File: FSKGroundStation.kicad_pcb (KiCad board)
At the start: 4 copper layers, 100 x 82 mm, 206 parts, among them J1 FTSH-105-01-L-DV-K, J10 CX90B1-24P, J11 HTSW-102-07-G-S, J22 BWSMA-KWE-Z001, J23 SJ-3524-SMT, J24 HTSW-103-07-G-S, J25 PJ-063BH, J3 CX90B1-24P, J4 BWSMA-KWE-Z001, J5 BWSMA-KWE-Z001, J9 HTSW-102-07-G-S, Q1 BSS138, Q2 BSS138, U1 TPSM861253RDXR, U10 74LVC1GU04DRL, U2 CC1312R1F3RGZR, U3 CY7C65215-32LTXI, U4 CC1125RHBR, U5 GRF5604, U6 SKYA21003, U7 GRF5604, U8 TPD4E004DRYR, U9 SKYA21003, Y1 OW7EL89CENUYO3YLC-40M, Y2 OW7EL89CANUXK7YLC-48M

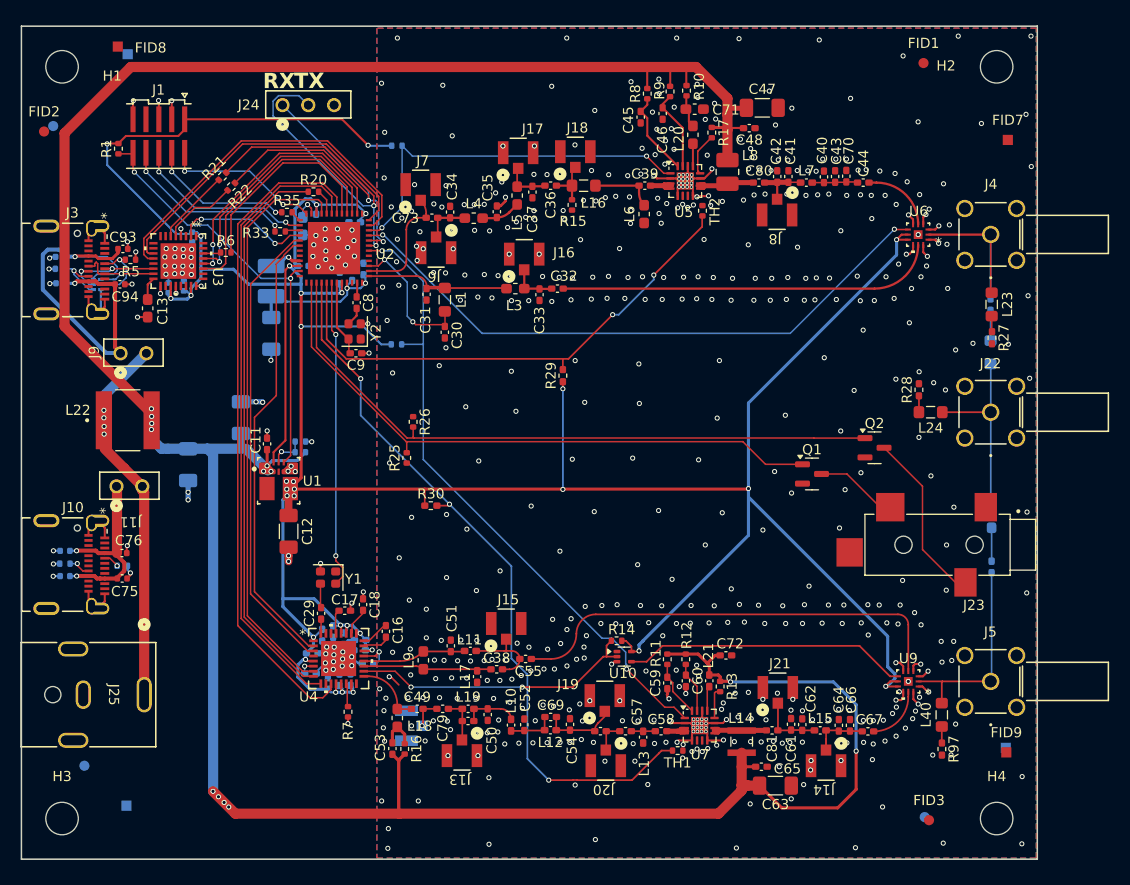
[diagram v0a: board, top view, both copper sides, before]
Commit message: Increase the board width to 82.5mm
To be sure it will work in the chassis.

Signed-off-by: Corey Minyard <corey@minyard.net>
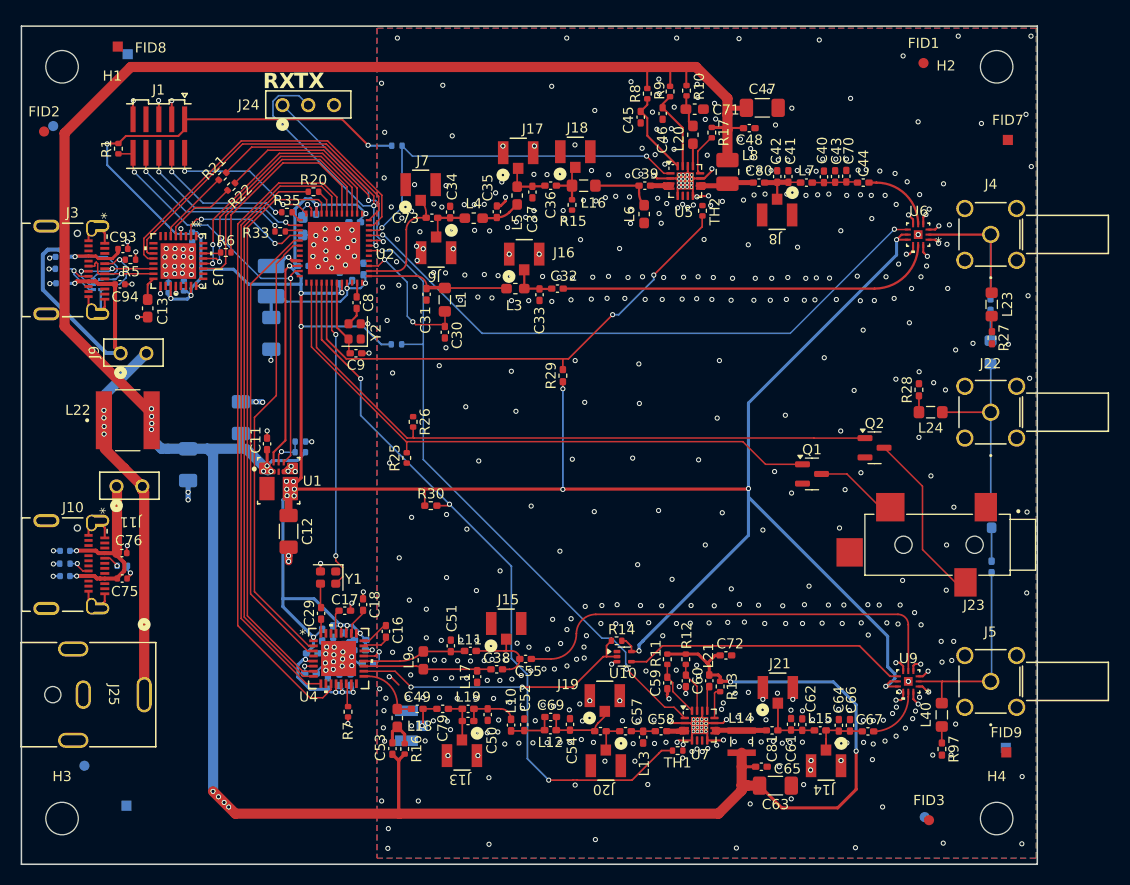
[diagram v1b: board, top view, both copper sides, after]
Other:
- board size 100 x 82 mm -> 100 x 82.5 mm
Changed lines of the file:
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@@
 	)
 	(gr_line
-		(start 170 140)
+		(start 170 140.5)
 		(end 170 58)
 		(stroke
 			(width 0.15)
-			(type default)
+			(type solid)
 		)
 		(locked yes)
@@
 	(gr_line
 		(start 70 58)
-		(end 70 140)
+		(end 70 140.5)
 		(stroke
 			(width 0.15)
-			(type default)
+			(type solid)
 		)
 		(locked yes)
@@
 	)
 	(gr_line
-		(start 70 140)
-		(end 170 140)
+		(start 70 140.5)
+		(end 170 140.5)
 		(stroke
 			(width 0.15)

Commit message: Increase the board width to 83mm
The slot it's supposed to go into is 84mm wide, it appears 82mm in the
middle.  83mm should be good.

According to a post on Amazon, the length is 103mm total with the inside
dimension 100mm.

Signed-off-by: Corey Minyard <corey@minyard.net>
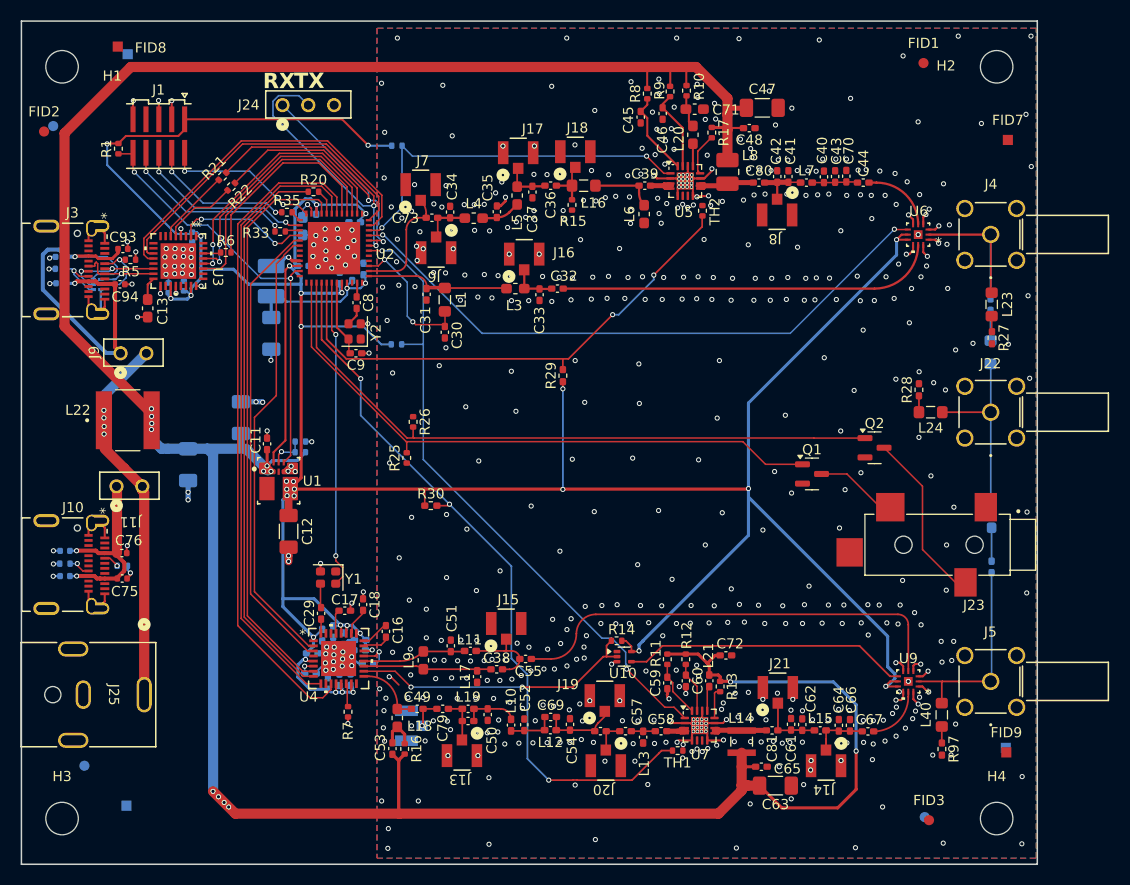
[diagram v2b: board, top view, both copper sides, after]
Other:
- board size 100 x 82.5 mm -> 100 x 83 mm
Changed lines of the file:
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@@
 	(gr_line
 		(start 170 140.5)
-		(end 170 58)
+		(end 170 57.5)
 		(stroke
 			(width 0.15)
@@
 	)
 	(gr_line
-		(start 70 58)
+		(start 70 57.5)
 		(end 70 140.5)
 		(stroke
@@
 	)
 	(gr_line
-		(start 170 58)
-		(end 70 58)
+		(start 170 57.5)
+		(end 70 57.5)
 		(stroke
 			(width 0.15)
-			(type default)
+			(type solid)
 		)
 		(locked yes)

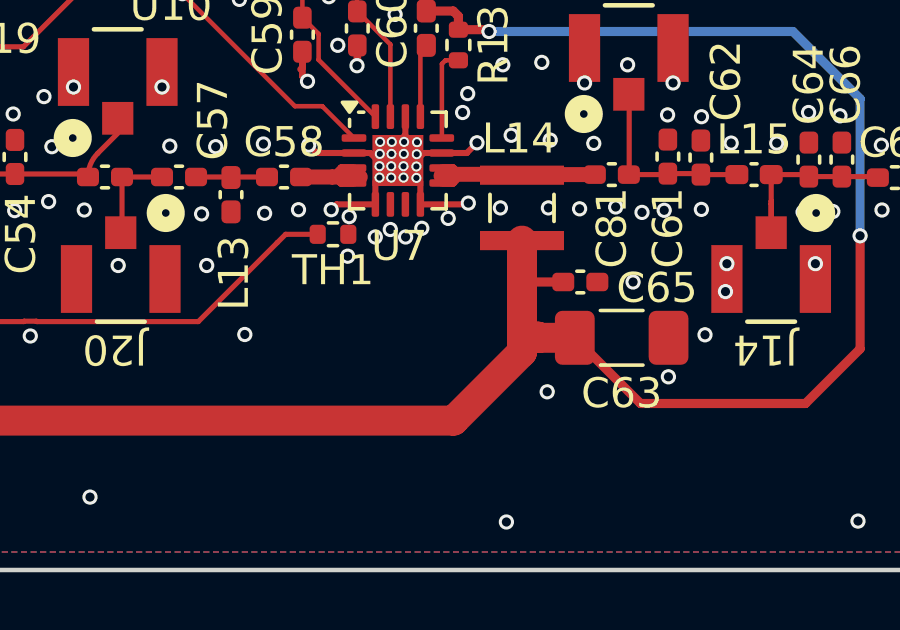
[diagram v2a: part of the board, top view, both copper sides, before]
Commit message: Add some more notes on heat sink options
Signed-off-by: Corey Minyard <corey@minyard.net>
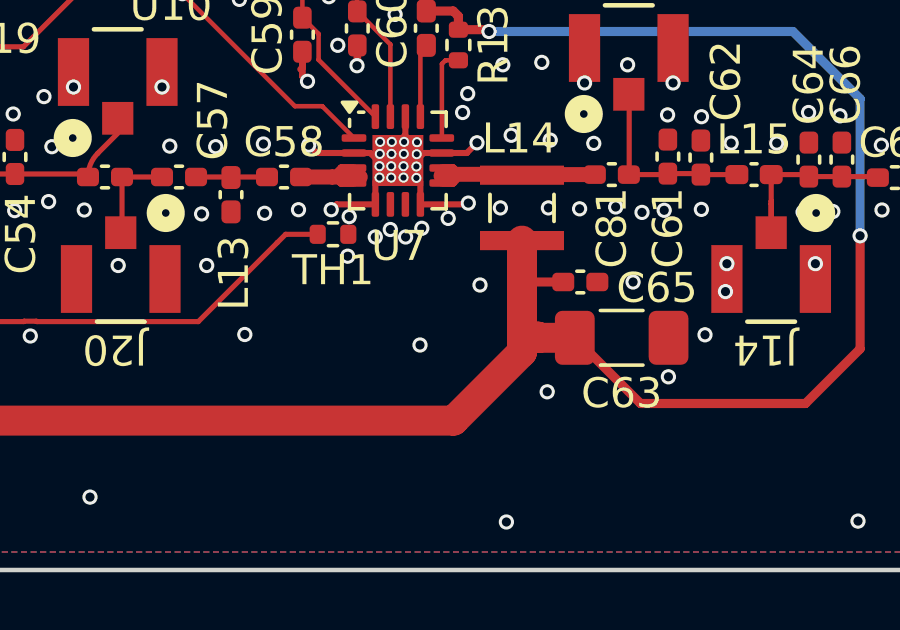
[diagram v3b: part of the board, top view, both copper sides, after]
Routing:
- net GND: vias 613 -> 615

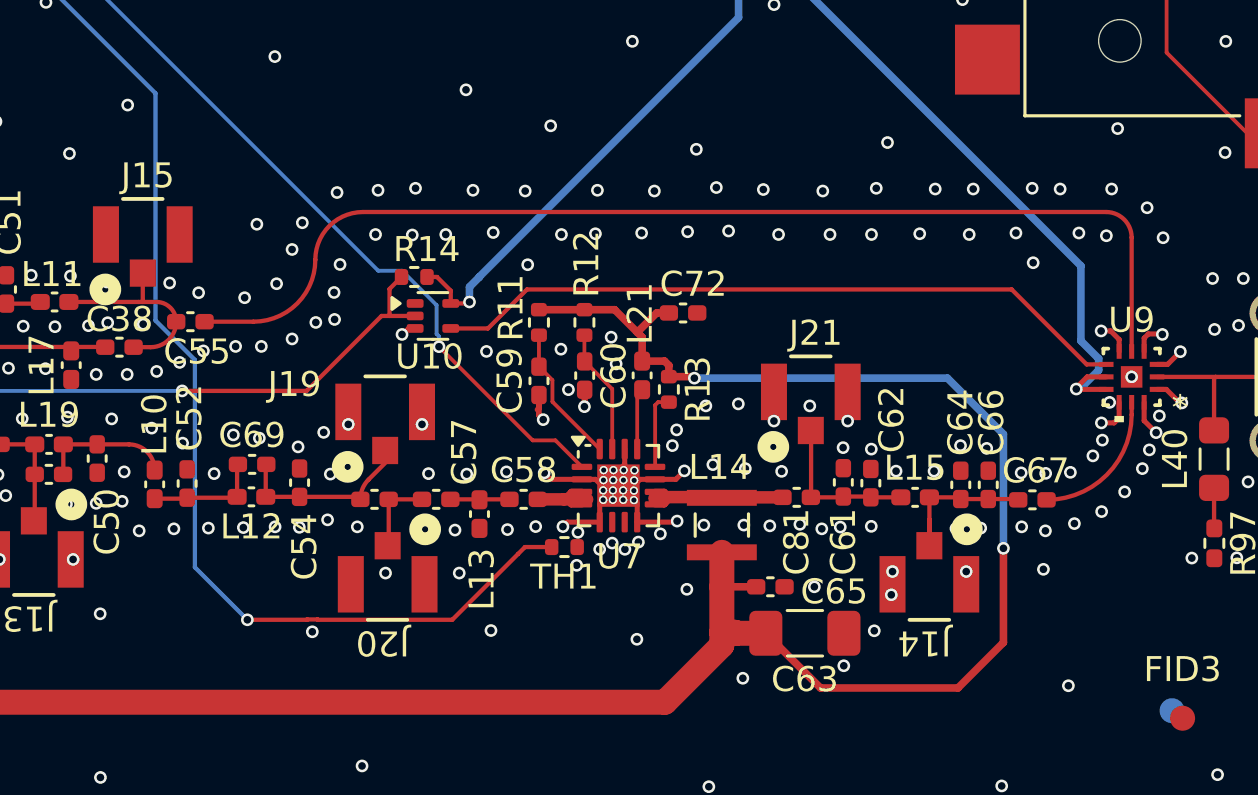
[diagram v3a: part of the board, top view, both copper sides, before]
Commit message: Rework the cc1125 matching networks
Per combining information from the 169MHz PA design (to separate the PA
and LNA outputs) and the 440 design (to get the component values).

Signed-off-by: Corey Minyard <corey@minyard.net>
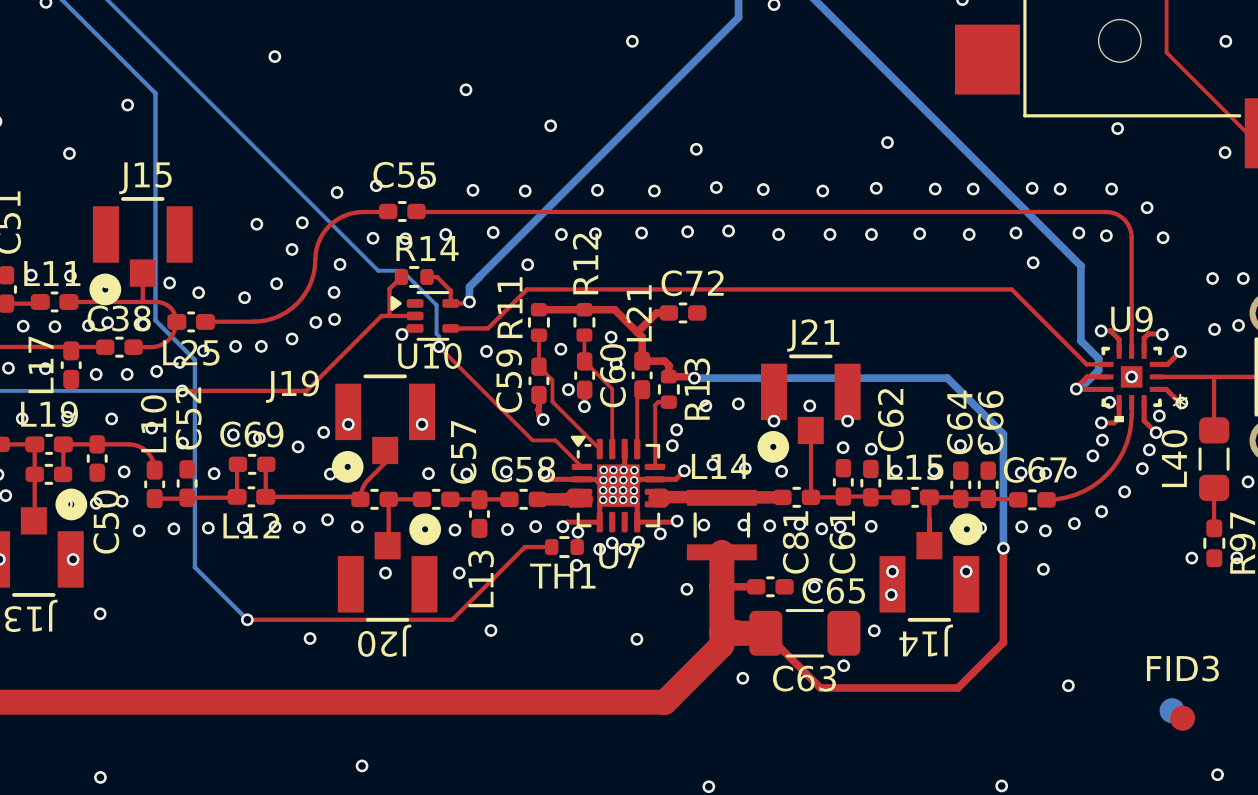
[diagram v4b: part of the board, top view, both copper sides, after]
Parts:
- removed C54: 12pF 1%, Capacitor_SMD:C_0402_1005Metric_Pad0.74x0.62mm_HandSolder
- added L25: 15nH 2%, Inductor_SMD:L_0402_1005Metric_Pad0.77x0.64mm_HandSolder, F.Cu at (119.7, 120.3)
- C50: value 15pF 1% -> 5.1pF 1%
- C52: value 2.2pF 1% -> 6.2pF 1%
- moved C55 9.56 mm to (128.1, 115.9)
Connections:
- C55 pad 1: Net-(J15-In) -> Net-(C55-Pad1)
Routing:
- net /440MHz/440_RX: track 44.5 -> 33.7 mm
- net Net-(C55-Pad1): track 0.00 -> 9.70 mm

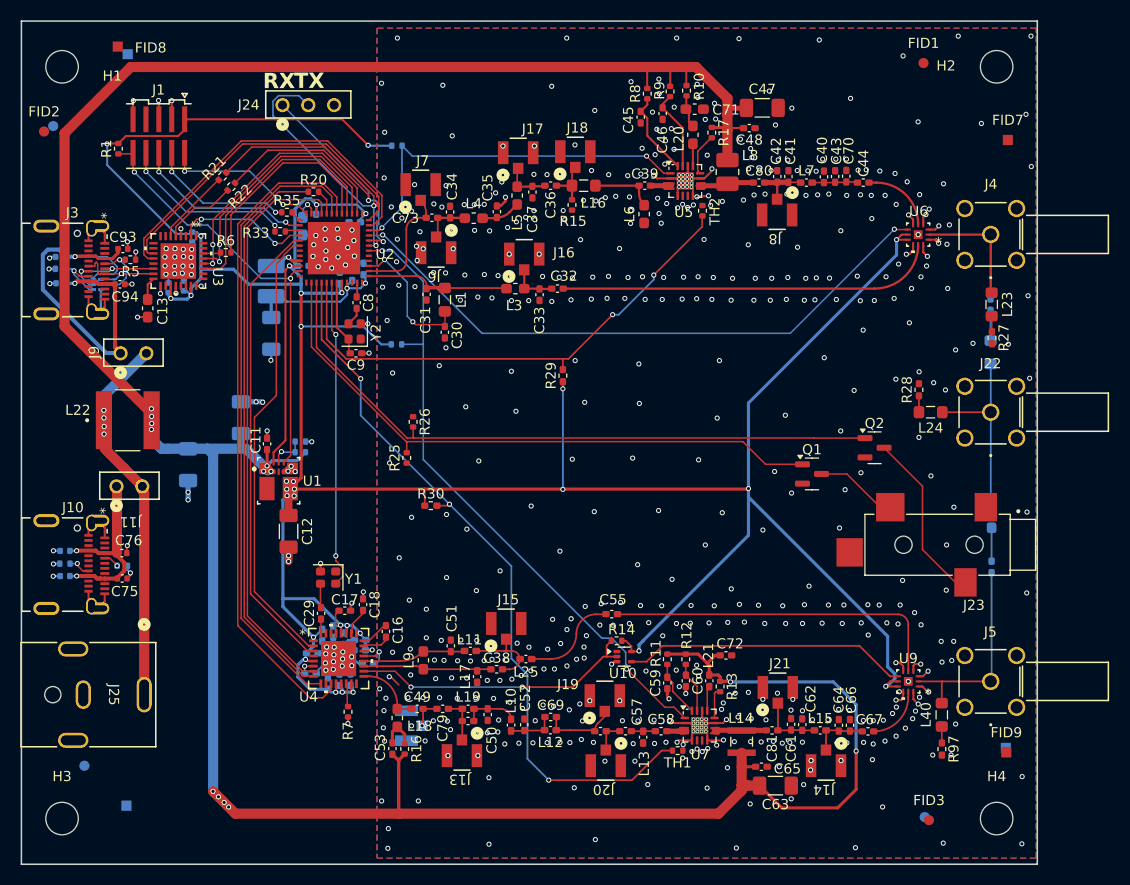
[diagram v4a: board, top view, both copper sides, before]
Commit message: Control the 440 switch directly from the CPU
The RX/TX switch on the CC1125 added a lot of complexity with the inverter
and such.  Instead, just drive it frmo the CC1125.

Use the RX/TX switch on the CC1125 as an option shown on the design with
169MHz and an external PA, not populated.

Signed-off-by: Corey Minyard <corey@minyard.net>
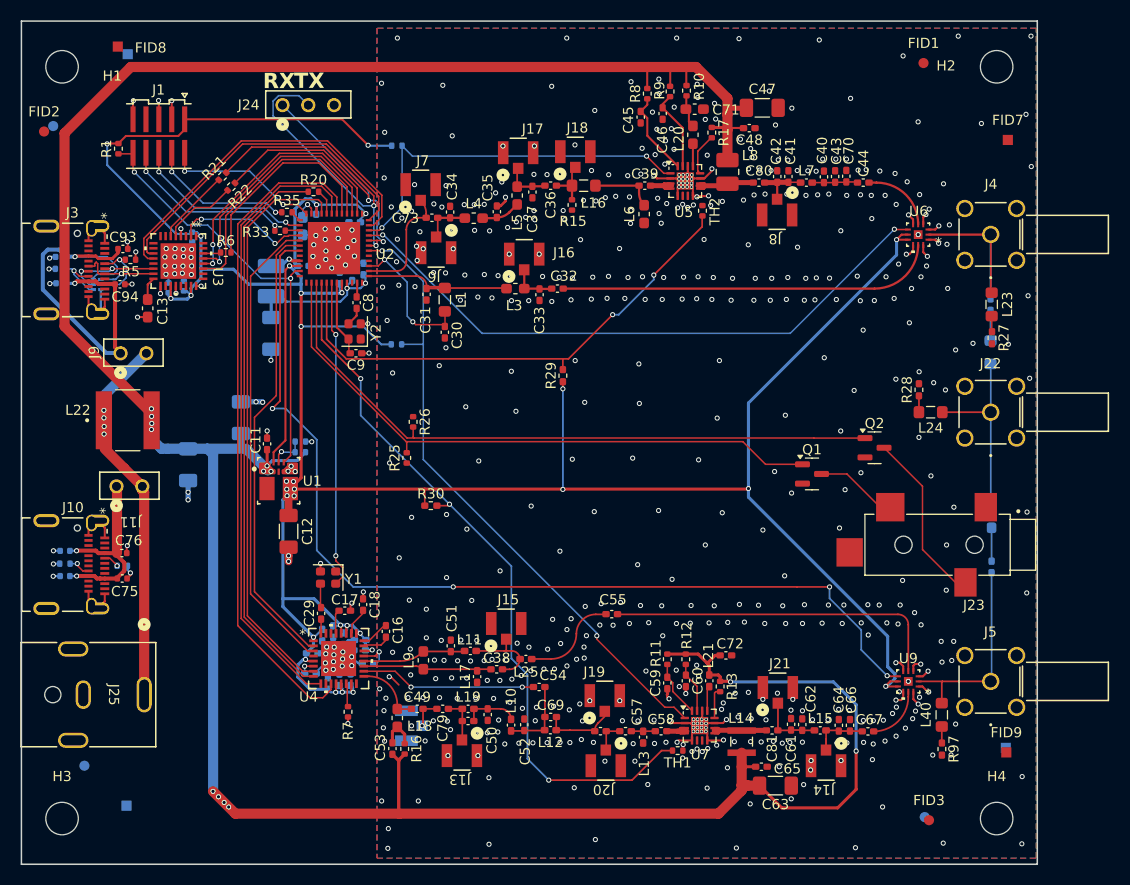
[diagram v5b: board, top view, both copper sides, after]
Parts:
- removed R14: 10K, Resistor_SMD:R_0402_1005Metric
- removed U10: 74LVC1GU04DRL, Package_TO_SOT_SMD:SOT-553
- added C54: 0, Capacitor_SMD:C_0402_1005Metric_Pad0.74x0.62mm_HandSolder, F.Cu at (121.0, 123.0)
- moved R33 0.08 mm to (95.5, 78.1)
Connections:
- U2 pad 31: unconnected-(U2-DIO_21-Pad31) -> 440_SWITCH
- U9 pad 7: Net-(U9-CTRL) -> 440_SWITCH
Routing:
- net 440_SWITCH: track 0.00 -> 98.2 mm, vias 0 -> 4
- net Net-(U9-CTRL): track 28.1 -> 0.00 mm
- net +3.3V: track 340.6 -> 318.5 mm, vias 32 -> 31
- net 440_TRX_SW: track 28.6 -> 17.3 mm
- net Net-(C52-Pad2): track 4.49 -> 7.44 mm
- net GND: track 104.9 -> 104.2 mm, vias 615 -> 613
- net 440MHz_TX_ENABLE: track 63.5 -> 62.9 mm
- net RADIO2_RESET_N: track 44.2 -> 44.7 mm

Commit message: Add some miscellaneous vias
Signed-off-by: Corey Minyard <corey@minyard.net>
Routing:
- net GND: vias 613 -> 618
